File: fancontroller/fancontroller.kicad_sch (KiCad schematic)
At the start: 24 parts, among them J1 Power, J2 Serial Conn, M1 FAN0, M2 FAN0, M3 FAN0, M4 FAN0, M5 FAN0, M6 FAN0, SW1 SW_Push, U2 ESP32-WROOM-32, U3 AMS1117-3.3

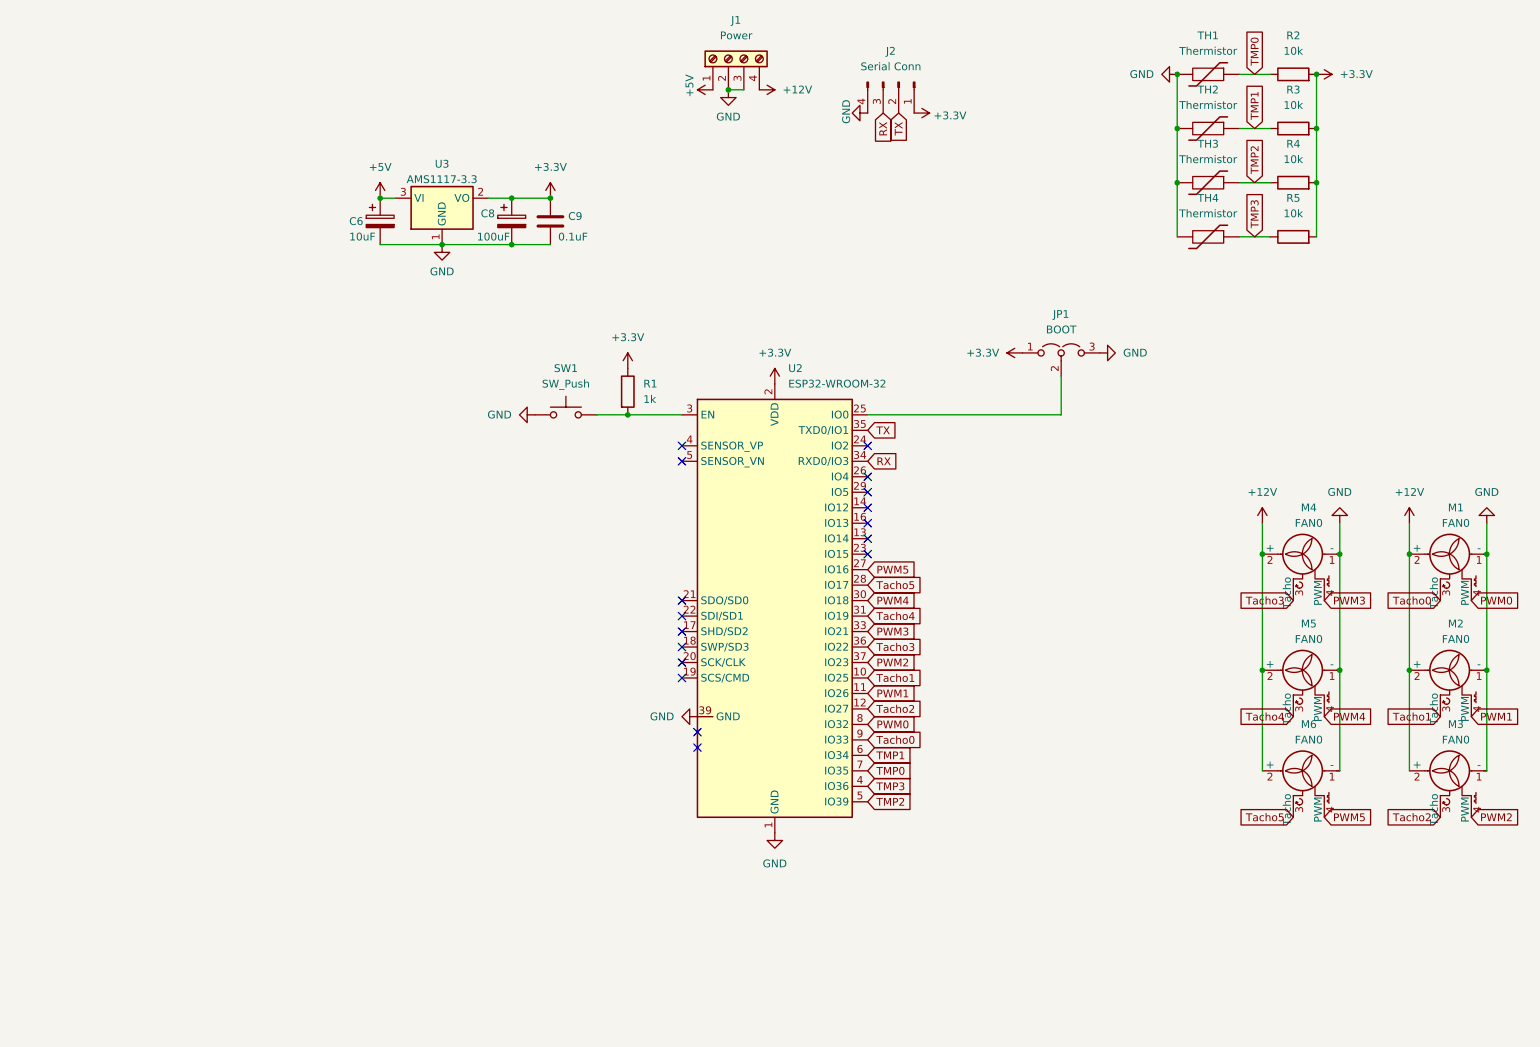
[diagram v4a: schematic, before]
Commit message: CMOS treiber für PWM output hinzugefügt, sicher ist sicher und extern pullup widerstände für Tacho inputs. Die sollten alle Teile für den ersten Prototypen sein.
PCB Layout muss angepasst werden und neu geroutet werden. Danach ready für ersten prototypen :)
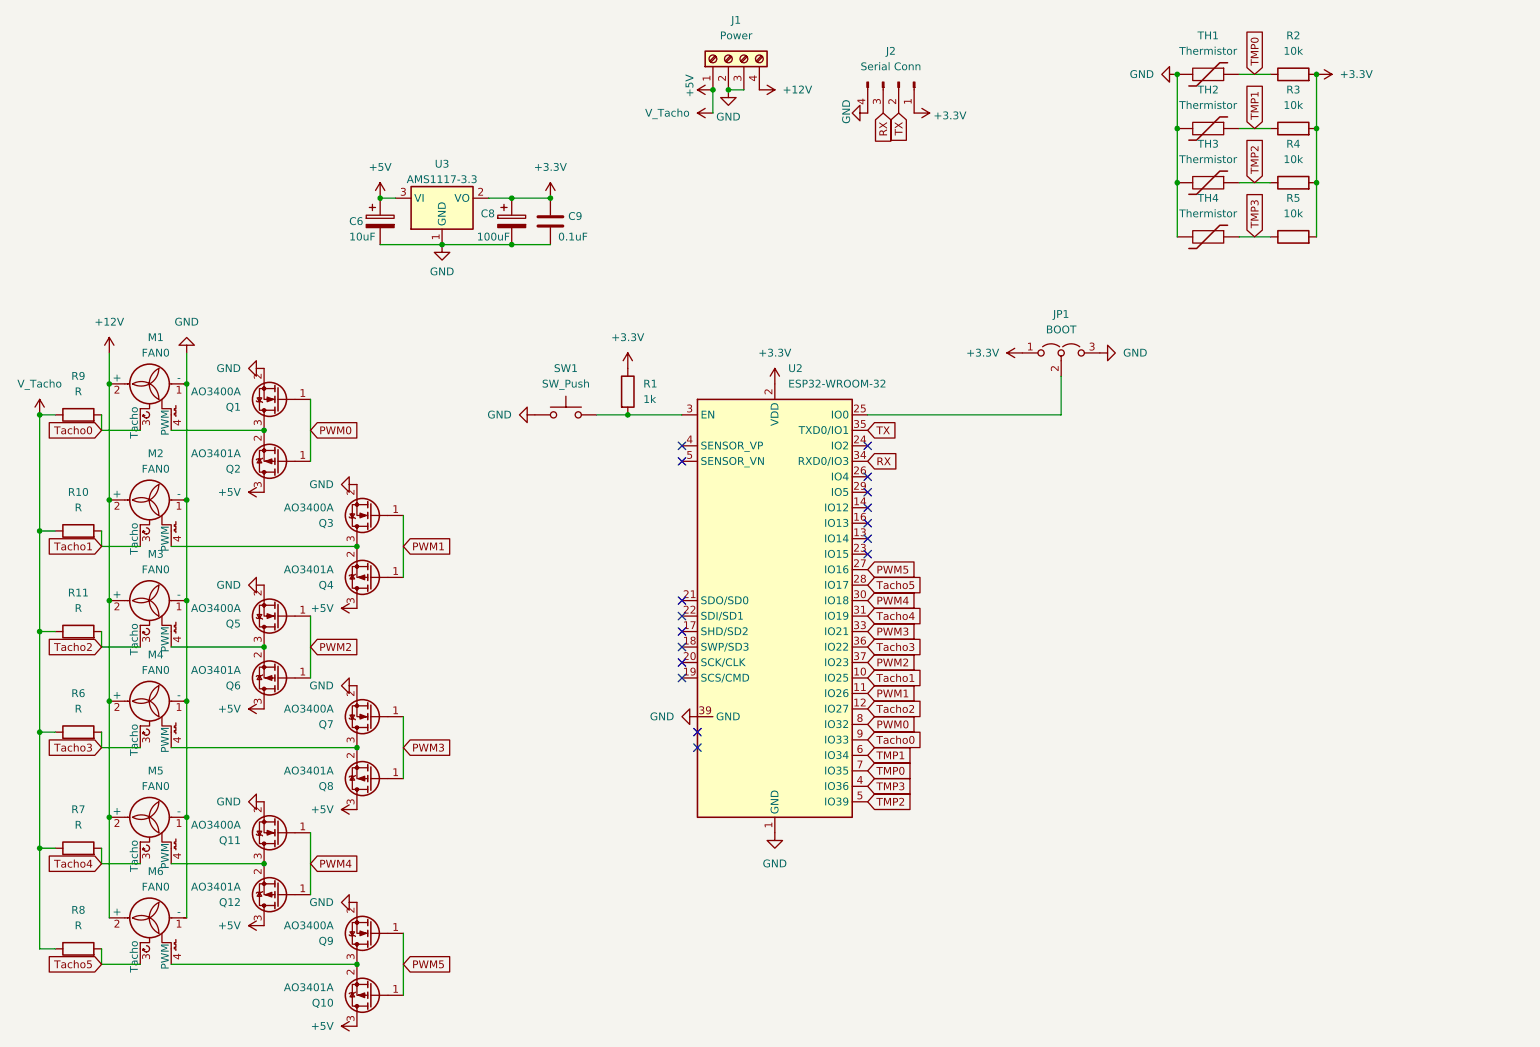
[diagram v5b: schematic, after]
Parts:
- added Q1, Q11, Q3, Q5, Q7, Q9: AO3400A, Package_TO_SOT_SMD:SOT-23, symbol Transistor_FET:AO3400A
- added Q10, Q12, Q2, Q4, Q6, Q8: AO3401A, Package_TO_SOT_SMD:SOT-23, symbol Transistor_FET:AO3401A
- added R10, R11, R6, R7, R8, R9: R, Resistor_SMD:R_0805_2012Metric, symbol Device:R
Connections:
- net +5V: now also Q10.3 (D), Q12.3 (D), Q2.3 (D), Q4.3 (D), Q6.3 (D), Q8.3 (D), R10.1, R11.1, R6.1, R7.1, R8.1, R9.1
- net GND: now also Q1.2 (S), Q11.2 (S), Q3.2 (S), Q5.2 (S), Q7.2 (S), Q9.2 (S)
- net PWM0: now also Q1.1 (G), Q2.1 (G); no longer M1.4 (PWM)
- net PWM1: now also Q3.1 (G), Q4.1 (G); no longer M2.4 (PWM)
- net PWM2: now also Q5.1 (G), Q6.1 (G); no longer M3.4 (PWM)
- net PWM3: now also Q7.1 (G), Q8.1 (G); no longer M4.4 (PWM)
- net PWM4: now also Q11.1 (G), Q12.1 (G); no longer M5.4 (PWM)
- net PWM5: now also Q10.1 (G), Q9.1 (G); no longer M6.4 (PWM)
- net Tacho0: now also R9.2
- net Tacho1: now also R10.2
- net Tacho2: now also R11.2
- net Tacho3: now also R6.2
- net Tacho4: now also R7.2
- net Tacho5: now also R8.2
- new net: M3.4 (PWM), Q5.3 (D), Q6.2 (S)
- new net: M6.4 (PWM), Q10.2 (S), Q9.3 (D)
- new net: M2.4 (PWM), Q3.3 (D), Q4.2 (S)
- new net: M5.4 (PWM), Q11.3 (D), Q12.2 (S)
- new net: M1.4 (PWM), Q1.3 (D), Q2.2 (S)
- new net: M4.4 (PWM), Q7.3 (D), Q8.2 (S)
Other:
- moved on the sheet: M1, M2, M3, M4, M5, M6

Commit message: Routing für ersten prototypen fertig und erste Teilnummern Parts zugeordnet für assembly preview
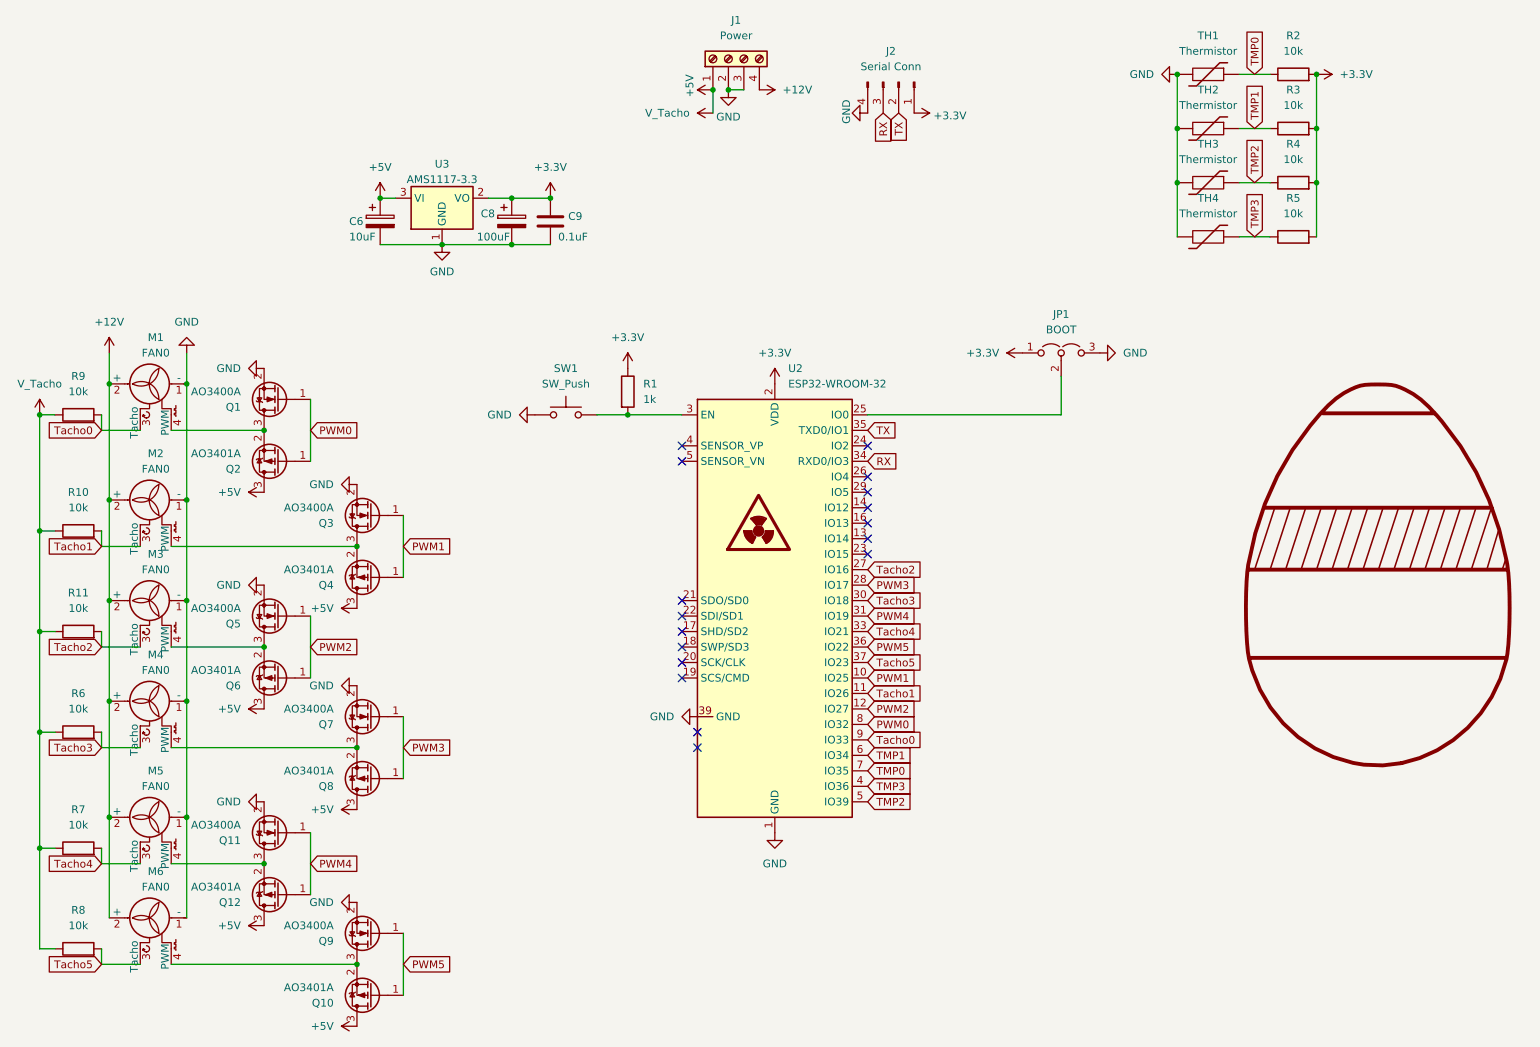
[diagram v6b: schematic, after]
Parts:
- added SYM1: SYM_EasterEgg_42x60mm, Symbol:Symbol_GNU-Logo_SilkscreenTop, symbol Graphic:SYM_EasterEgg_42x60mm
- J1: LCSC Part # (none) -> C915913
- J2: LCSC Part # (none) -> C5116483
- JP1: LCSC Part # (none) -> C27985188
- Q1, Q11, Q3, Q5, Q7, Q9: LCSC Part # (none) -> C20917
- Q10, Q12, Q2, Q4, Q6, Q8: LCSC Part # (none) -> C15127
- R1: LCSC Part # (none) -> C140871
- R10, R11, R6, R7, R8, R9: value R -> 10k; LCSC Part # (none) -> C365230
- R2, R3, R4, R5: LCSC Part # (none) -> C365230
- SW1, TH1, TH2, TH3, TH4: LCSC Part # (none) -> C5360898
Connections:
- net PWM1: now also U2.10 (IO25); no longer U2.11 (IO26)
- net PWM2: now also U2.12 (IO27); no longer U2.37 (IO23)
- net PWM3: now also U2.28 (IO17); no longer U2.33 (IO21)
- net PWM4: now also U2.31 (IO19); no longer U2.30 (IO18)
- net PWM5: now also U2.36 (IO22); no longer U2.27 (IO16)
- net Tacho1: now also U2.11 (IO26); no longer U2.10 (IO25)
- net Tacho2: now also U2.27 (IO16); no longer U2.12 (IO27)
- net Tacho3: now also U2.30 (IO18); no longer U2.36 (IO22)
- net Tacho4: now also U2.33 (IO21); no longer U2.31 (IO19)
- net Tacho5: now also U2.37 (IO23); no longer U2.28 (IO17)

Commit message: JLCPCB order rotations fixed for most parts
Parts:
- C6: footprint Capacitor_THT:CP_Radial_D4.0mm_P1.50mm -> Capacitor_SMD:C_0805_2012Metric; LCSC Part # (none) -> C440198
- C8: footprint Capacitor_THT:CP_Radial_D5.0mm_P2.00mm -> Capacitor_SMD:CP_Elec_10x10; JLCPCB Rotation Offset (none) -> 180; LCSC Part # (none) -> C249836
- C9: footprint Capacitor_THT:C_Disc_D3.0mm_W2.0mm_P2.50mm -> Capacitor_SMD:C_0805_2012Metric; LCSC Part # (none) -> C49678
- J1, J2, SW1, TH1, TH2, TH3, TH4: JLCPCB Rotation Offset (none) -> 90
- JP1: JLCPCB Rotation Offset (none) -> -90
- M1, M2, M3, M4, M5, M6: JLCPCB Rotation Offset (none) -> 90; LCSC Part # (none) -> C402778
- R1: LCSC Part # C140871 -> C17513
- R10, R11, R2, R3, R4, R5, R6, R7, R8, R9: LCSC Part # C365230 -> C17414

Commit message: prepare to start dev on v1.2
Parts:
- removed SYM1: SYM_EasterEgg_42x60mm, Symbol:Symbol_GNU-Logo_SilkscreenTop, symbol Graphic:SYM_EasterEgg_42x60mm
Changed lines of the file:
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@@
-	)
-	(symbol
-		(lib_id "Graphic:SYM_EasterEgg_42x60mm")
-		(at 240.03 144.78 0)
-		(unit 1)
-		(exclude_from_sim yes)
-		(in_bom no)
-		(on_board yes)
-		(dnp no)
-		(fields_autoplaced yes)
-		(property "Reference" "SYM1"
-			(at 240.03 144.78 0)
-			(effects
-				(font
-					(size 1.27 1.27)
-				)
-				(hide yes)
-			)
-		)
-		(property "Value" "SYM_EasterEgg_42x60mm"
-			(at 240.03 144.78 0)
-			(effects
-				(font
-					(size 1.27 1.27)
-				)
-				(hide yes)
-			)
-		)
-		(property "Footprint" "Symbol:Symbol_GNU-Logo_SilkscreenTop"
-			(at 240.03 148.59 0)
-			(effects
-				(font
-					(size 1.27 1.27)
-				)
-				(hide yes)
-			)
-		)
-		(property "Datasheet" "https://eur-lex.europa.eu/LexUriServ/LexUriServ.do?uri=OJ:L:2013:347:0671:0854:de:PDF"
-			(at 240.03 151.13 0)
-			(effects
-				(font
-					(size 1.27 1.27)
-				)
-				(hide yes)
-			)
-		)
-		(property "Description" "EasterEgg, ClassA, Medium Size"
-			(at 240.03 144.78 0)
-			(effects
-				(font
-					(size 1.27 1.27)
-				)
-				(hide yes)
-			)
-		)
-		(property "LCSC Part #" ""
-			(at 240.03 144.78 0)
-			(effects
-				(font
-					(size 1.27 1.27)
-				)
-				(hide yes)
-			)
-		)
-		(property "JLCPCB Rotation Offset" ""
-			(at 240.03 144.78 0)
-			(effects
-				(font
-					(size 1.27 1.27)
-				)
-				(hide yes)
-			)
-		)
-		(instances
-			(project ""
-				(path "/0224fd83-71fd-467a-bea0-55e2843206f4"
-					(reference "SYM1")
-					(unit 1)
-				)
-			)
-		)
 	)
 	(symbol
